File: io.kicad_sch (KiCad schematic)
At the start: 2 parts

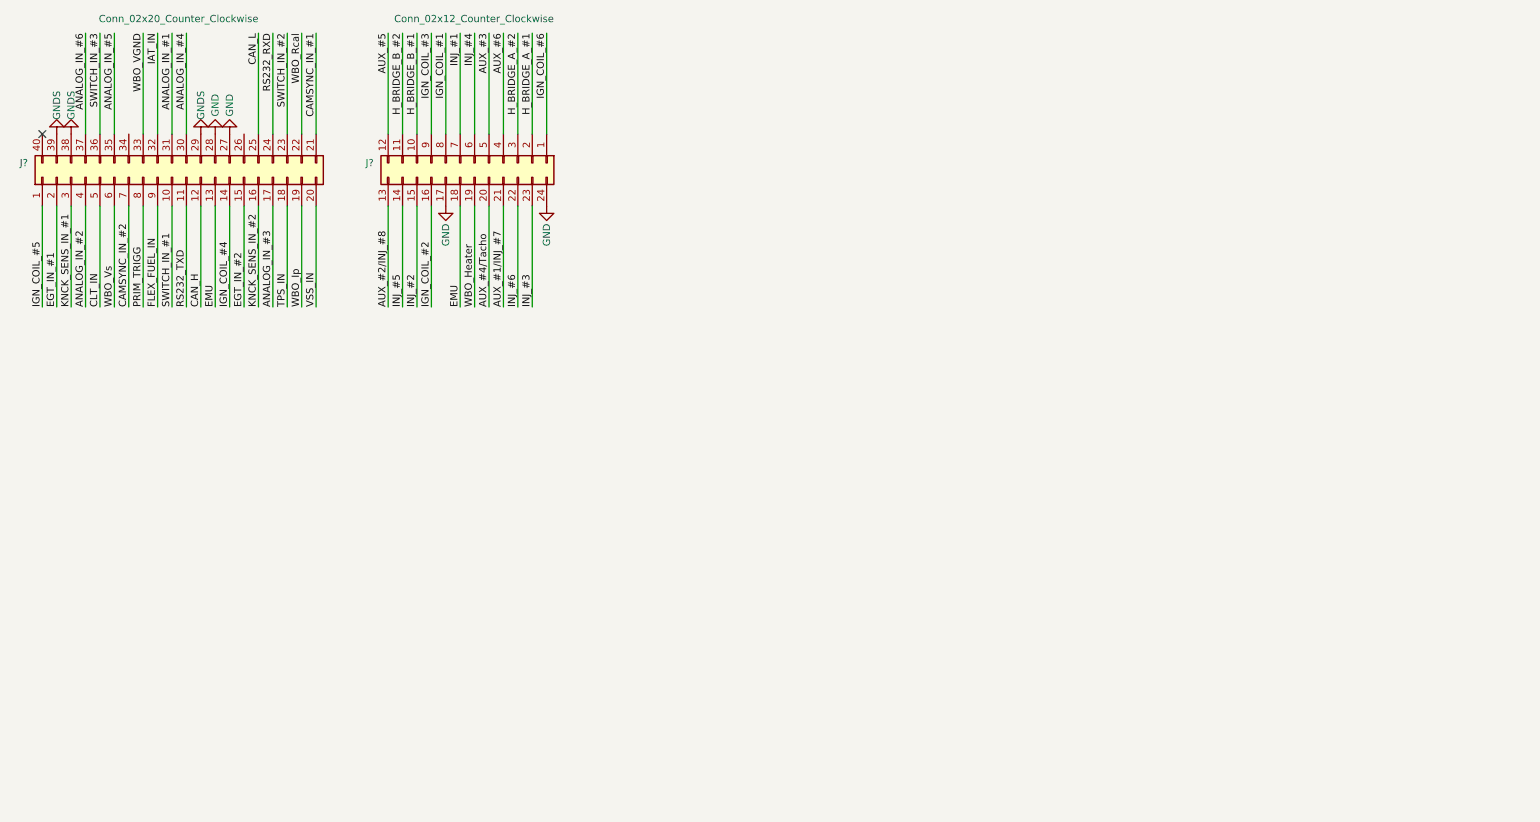
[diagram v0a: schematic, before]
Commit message: Expanded IO
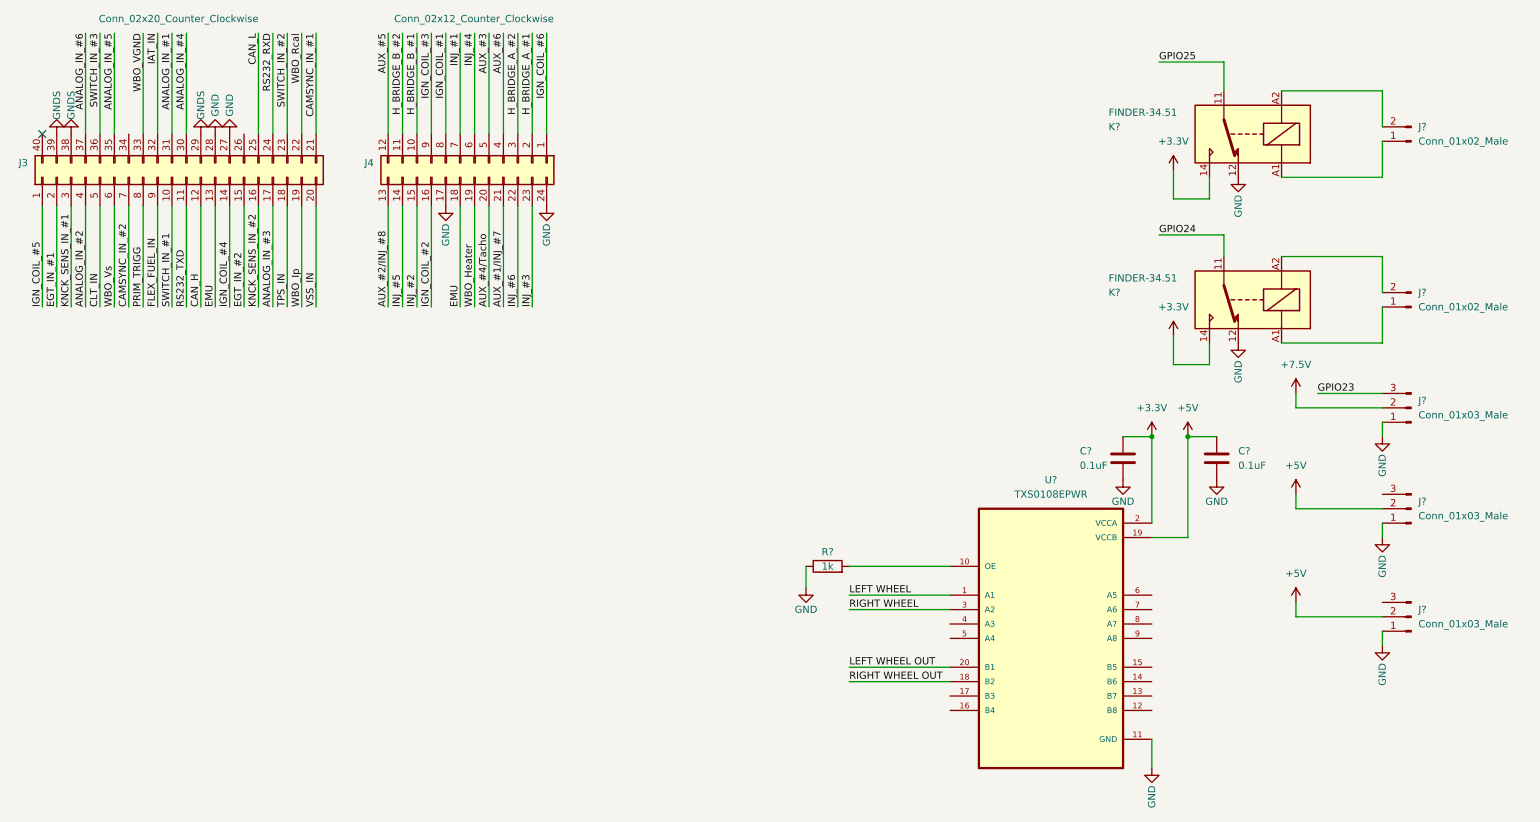
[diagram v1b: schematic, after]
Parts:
- added C? (x2): 0.1uF, symbol Device:C
- added J? (x2): Conn_01x02_Male, symbol Connector:Conn_01x02_Male
- added J? (x3): Conn_01x03_Male, symbol Connector:Conn_01x03_Male
- added K? (x2): FINDER-34.51, Relay_THT:Relay_SPDT_Finder_34.51_Vertical, symbol Relay:FINDER-34.51
- added R?: 1k, symbol Device:R
- added U?: TXS0108EPWR, SOP65P640X120-20N, symbol TXS0108EPWR:TXS0108EPWR
- gave numbers to parts that had none: 2
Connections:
- net GND: now also C?.1, C?.1, J?.1 (Pin_1), J?.1 (Pin_1), J?.1 (Pin_1), K?.12, K?.12, R?.1, U?.11 (GND)
- new net: J?.1 (Pin_1), K?.A1 (x2)
- new net: J?.2 (Pin_2), K?.A2 (x2)
- new net: R?.2, U?.10 (OE)
- new net +3.3V: C?.2, K?.14, K?.14, U?.2 (VCCA)
- new net +5V: C?.2, J?.2 (Pin_2), J?.2 (Pin_2), U?.19 (VCCB)
- new net +7.5V: J?.2 (Pin_2)
- new net GPIO23: J?.3 (Pin_3)
- new net GPIO24: K?.11
- new net GPIO25: K?.11
- new net LEFT WHEEL: U?.1 (A1)
- new net LEFT WHEEL OUT: U?.20 (B1)
- new net RIGHT WHEEL: U?.3 (A2)
- new net RIGHT WHEEL OUT: U?.18 (B2)

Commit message: Rev 1.0
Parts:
- added D10, D9: ES1J, ES1J:DIO_ES1J, symbol ES1J:ES1J
- added J11: STARTER CON, AMASS_XT60PW-F:AMASS_XT60PW-F, symbol XT60PW-F:XT60PW-F
- added J12, J13: USB_C_Receptacle, Connector_USB:USB_C_Receptacle_HRO_TYPE-C-31-M-12, symbol Connector:USB_C_Receptacle
- added J14: CAN, Connector_Molex:Molex_PicoBlade_53047-0210_1x02_P1.25mm_Vertical, symbol Connector:Conn_01x02_Male
- added J15: 3.3V OUT, Connector_Molex:Molex_PicoBlade_53047-0210_1x02_P1.25mm_Vertical, symbol Connector:Conn_01x02_Male
- added J16: 5V OUT, Connector_Molex:Molex_PicoBlade_53047-0210_1x02_P1.25mm_Vertical, symbol Connector:Conn_01x02_Male
- added J17: 7.5V OUT, Connector_Molex:Molex_PicoBlade_53047-0210_1x02_P1.25mm_Vertical, symbol Connector:Conn_01x02_Male
- added J18: OIL CON, Connector_Molex:Molex_PicoBlade_53047-0210_1x02_P1.25mm_Vertical, symbol Connector:Conn_01x02_Male
- added J19: IAT CON, Connector_Molex:Molex_PicoBlade_53047-0210_1x02_P1.25mm_Vertical, symbol Connector:Conn_01x02_Male
- added J20: PRIM TRIGG CON, Connector_Molex:Molex_PicoBlade_53047-0210_1x02_P1.25mm_Vertical, symbol Connector:Conn_01x02_Male
- added J21: SEC TRIGG CON, Connector_Molex:Molex_PicoBlade_53047-0210_1x02_P1.25mm_Vertical, symbol Connector:Conn_01x02_Male
- added J22: EGT CON, Connector_Molex:Molex_PicoBlade_53047-0210_1x02_P1.25mm_Vertical, symbol Connector:Conn_01x02_Male
- added J23: DATA LOGGER CON, Connector_Molex:Molex_PicoBlade_53047-0310_1x03_P1.25mm_Vertical, symbol Connector:Conn_01x03_Male
- added J24: IGN CON, Connector_Molex:Molex_PicoBlade_53047-0310_1x03_P1.25mm_Vertical, symbol Connector:Conn_01x03_Male
- added J25: INJ CON, Connector_Molex:Molex_PicoBlade_53047-0210_1x02_P1.25mm_Vertical, symbol Connector:Conn_01x02_Male
- added K3: FINDER-34.51 INJ, Relay_THT:Relay_SPDT_Finder_34.51_Vertical, symbol Relay:FINDER-34.51
- added Q2, Q3, Q4: IRFP1405PBF, IRFP1405:TO247AC, symbol IRFP1405:IRFP1405PBF
- added R16: 330, Resistor_SMD:R_0603_1608Metric, symbol Device:R
- added U8: 2EDN7524F, 2EDN7524F:SOIC127P600X175-8N-22-V, symbol 2EDN7524F:2EDN7524F
- C15, C16: renamed from C?; footprint (none) -> Capacitor_SMD:C_0201_0603Metric
- J10: renamed from J?; value Conn_01x03_Male -> RIGHT WHEEL SENS; footprint (none) -> Connector_Molex:Molex_PicoBlade_53047-0310_1x03_P1.25mm_Vertical
- J3: value Conn_02x20_Counter_Clockwise -> EMU_BLACK_A; footprint (none) -> Connector_PinHeader_2.54mm:PinHeader_2x20_P2.54mm_Vertical
- J4: value Conn_02x12_Counter_Clockwise -> EMU_BLACK_B; footprint (none) -> Connector_PinHeader_2.54mm:PinHeader_2x12_P2.54mm_Vertical
- J6: renamed from J?; value Conn_01x02_Male -> INJ CON; footprint (none) -> Connector_Molex:Molex_PicoBlade_53047-0210_1x02_P1.25mm_Vertical
- J7: renamed from J?; value Conn_01x02_Male -> STARTER INF; footprint (none) -> Connector_Molex:Molex_PicoBlade_53047-0210_1x02_P1.25mm_Vertical
- J8: renamed from J?; value Conn_01x03_Male -> SERVO; footprint (none) -> Connector_Molex:Molex_PicoBlade_53047-0310_1x03_P1.25mm_Vertical
- J9: renamed from J?; value Conn_01x03_Male -> LEFT WHEEL SENS; footprint (none) -> Connector_Molex:Molex_PicoBlade_53047-0310_1x03_P1.25mm_Vertical
- K1: renamed from K?; value FINDER-34.51 -> FINDER-34.51 INJ
- K2: renamed from K?; value FINDER-34.51 -> FINDER-34.51 STARTER
- R14: renamed from R?; footprint (none) -> Resistor_SMD:R_0603_1608Metric
- U7: renamed from U?; footprint SOP65P640X120-20N -> TXS0108EPWR:SOP65P640X120-20N
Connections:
- net +3.3V: now also J15.2 (Pin_2)
- net +5V: now also J16.2 (Pin_2), U8.6 (VDD)
- net +7.5V: now also J17.2 (Pin_2)
- net ANALOG_IN_#1: now also J18.2 (Pin_2), R16.1
- net CAMSYNC_IN_#1: now also J21.2 (Pin_2)
- net CAN_H: now also J14.1 (Pin_1)
- net CAN_L: now also J14.2 (Pin_2)
- net EGT_IN_#1: now also J22.2 (Pin_2)
- net GND: now also J15.1 (Pin_1), J16.1 (Pin_1), J17.1 (Pin_1), J24.1 (Pin_1), Q2.3 (S), Q3.3 (S), Q4.3 (S)
- net GNDS: now also J18.1 (Pin_1), J19.1 (Pin_1), J20.1 (Pin_1), J21.1 (Pin_1), J22.1 (Pin_1), J23.3 (Pin_3)
- net IAT_IN: now also J19.2 (Pin_2)
- net IGN_COIL_#1: now also J24.2 (Pin_2)
- net INJ_#1: now also K3.14
- net LEFT WHEEL OUT: now also J9.3 (Pin_3)
- net PRIM_TRIGG: now also J20.2 (Pin_2)
- net RIGHT WHEEL OUT: now also J10.3 (Pin_3)
- net RS232_TXD: now also J23.2 (Pin_2)
- net INJ IN: now reaches J6.1 (Pin_1), K1.A1
- net INJ IN: now also D9.K, K3.A1
- net INJ OUT: now reaches J6.2 (Pin_2), K1.A2
- net INJ OUT: now also D9.A, K3.A2
- net at J7.1 (Pin_1), K2.A1: now also D10.K
- net at J7.2 (Pin_2), K2.A2: now also D10.A
- net 5V EMU: now reaches J3.26 (Pin_26)
- net 5V EMU: now also J3.34 (Pin_34), J23.1 (Pin_1), R16.2
- new net: Q2.1 (G), Q3.1 (G), Q4.1 (G), U8.7 (OUTA)
- new net: J11.2, Q2.2 (D), Q3.2 (D), Q4.2 (D)
- new net: J11.S1 (SHIELD), J11.S2 (SHIELD)
- new net: J25.1 (Pin_1), K3.11
- new net: J12.A1 (GND), J12.A12 (GND), J12.B1 (GND), J12.B12 (GND), J12.S1 (SHIELD)
- new net GPIO22: U8.2 (INA)
- new net IGN: J24.3 (Pin_3)
- new net INJ: J25.2 (Pin_2)
- new net STARTER: J11.1
- new net USB_PASSTHROUH_DN: J12.A7 (D-), J12.B7 (D-), J13.A7 (D-), J13.B7 (D-)
- new net USB_PASSTHROUH_DP: J12.A6 (D+), J12.B6 (D+), J13.A6 (D+), J13.B6 (D+)
- new net USB_PASSTHROUH_GND: J13.A1 (GND), J13.A12 (GND), J13.B1 (GND), J13.B12 (GND), J13.S1 (SHIELD)
- new net USB_PASSTHROUH_VSYS: J12.A4 (VBUS), J12.A9 (VBUS), J12.B4 (VBUS), J12.B9 (VBUS), J13.A4 (VBUS), J13.A9 (VBUS), J13.B4 (VBUS), J13.B9 (VBUS)
- no-connect marks 1 -> 19
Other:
- title: (none) -> Iron Warriors v2.0 
- moved on the sheet: C15, C16, J10, J6, J7, J8, J9, K1, K2, R14, U7

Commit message: Initial PCB view
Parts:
- C15, C16: footprint Capacitor_SMD:C_0201_0603Metric -> Capacitor_SMD:C_0603_1608Metric
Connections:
- net RIGHT WHEEL is gone; now on net GPIO22: U7.3 (A2)
- net GPIO22: no longer U8.2 (INA)
- net GPIO23: now also U8.2 (INA); no longer J8.3 (Pin_3)
- net LEFT WHEEL renamed GPIO21
- new net GPIO20: J8.3 (Pin_3)
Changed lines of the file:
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@@
   (title_block
     (title "Iron Warriors v2.0 ")
-    (date "2022-12-08")
+    (date "2022-12-13")
     (rev "1.0")
   )
@@
     (stroke (width 0) (type default) (color 0 0 0 0))
   )
-  (wire (pts (xy 365.76 113.03) (xy 365.76 115.57))
-    (stroke (width 0) (type default) (color 0 0 0 0))
-  )
   (wire (pts (xy 344.17 78.74) (xy 350.52 78.74))
     (stroke (width 0) (type default) (color 0 0 0 0))
@@
     (stroke (width 0) (type default) (color 0 0 0 0))
   )
+  (wire (pts (xy 359.41 113.665) (xy 359.41 115.57))
+    (stroke (width 0) (type default) (color 0 0 0 0))
+  )
   (wire (pts (xy 326.39 179.07) (xy 326.39 173.99))
     (stroke (width 0) (type default) (color 0 0 0 0))
@@
     (stroke (width 0) (type default) (color 0 0 0 0))
   )
+  (wire (pts (xy 273.05 148.59) (xy 290.83 148.59))
+    (stroke (width 0) (type default) (color 0 0 0 0))
+  )
   (wire (pts (xy 381 157.48) (xy 381 154.94))
     (stroke (width 0) (type default) (color 0 0 0 0))
@@
     (stroke (width 0) (type default) (color 0 0 0 0))
   )
+  (wire (pts (xy 273.05 151.13) (xy 290.83 151.13))
+    (stroke (width 0) (type default) (color 0 0 0 0))
+  )
   (wire (pts (xy 323.85 209.55) (xy 340.36 209.55))
     (stroke (width 0) (type default) (color 0 0 0 0))
@@
     (stroke (width 0) (type default) (color 0 0 0 0))
   )
-  (wire (pts (xy 273.05 148.59) (xy 290.83 148.59))
-    (stroke (width 0) (type default) (color 0 0 0 0))
-  )
   (wire (pts (xy 195.58 43.18) (xy 195.58 25.4))
     (stroke (width 0) (type default) (color 0 0 0 0))
@@
     (stroke (width 0) (type default) (color 0 0 0 0))
   )
-  (wire (pts (xy 365.76 115.57) (xy 381 115.57))
-    (stroke (width 0) (type default) (color 0 0 0 0))
-  )
   (wire (pts (xy 107.95 68.58) (xy 107.95 50.8))
     (stroke (width 0) (type default) (color 0 0 0 0))
@@
     (stroke (width 0) (type default) (color 0 0 0 0))
   )
-  (wire (pts (xy 265.43 147.32) (xy 265.43 143.51))
+  (wire (pts (xy 257.81 147.32) (xy 257.81 143.51))
     (stroke (width 0) (type default) (color 0 0 0 0))
   )
@@
     (stroke (width 0) (type default) (color 0 0 0 0))
   )
-  (wire (pts (xy 265.43 143.51) (xy 270.51 143.51))
+  (wire (pts (xy 257.81 143.51) (xy 270.51 143.51))
     (stroke (width 0) (type default) (color 0 0 0 0))
   )
@@
     (stroke (width 0) (type default) (color 0 0 0 0))
   )
-  (wire (pts (xy 273.05 151.13) (xy 290.83 151.13))
-    (stroke (width 0) (type default) (color 0 0 0 0))
-  )
   (wire (pts (xy 208.28 43.18) (xy 208.28 25.4))
     (stroke (width 0) (type default) (color 0 0 0 0))
@@
     (stroke (width 0) (type default) (color 0 0 0 0))
   )
+  (wire (pts (xy 359.41 115.57) (xy 381 115.57))
+    (stroke (width 0) (type default) (color 0 0 0 0))
+  )
   (wire (pts (xy 71.12 96.52) (xy 46.99 96.52))
     (stroke (width 0) (type default) (color 0 0 0 0))
@@
     (effects (font (size 1.27 1.27)) (justify left bottom))
   )
-  (label "RIGHT WHEEL" (at 273.05 151.13 0)
+  (label "GPIO22" (at 273.05 151.13 0)
     (effects (font (size 1.27 1.27)) (justify left bottom))
   )
@@
     (effects (font (size 1.27 1.27)) (justify right bottom))
   )
-  (label "LEFT WHEEL" (at 273.05 148.59 0)
-    (effects (font (size 1.27 1.27)) (justify left bottom))
-  )
   (label "IGN_COIL_#1" (at 92.71 20.32 270)
     (effects (font (size 1.27 1.27)) (justify right bottom))
@@
     (effects (font (size 1.27 1.27)) (justify right bottom))
   )
+  (label "GPIO21" (at 273.05 148.59 0)
+    (effects (font (size 1.27 1.27)) (justify left bottom))
+  )
   (label "INJ_#5" (at 85.09 68.58 90)
     (effects (font (size 1.27 1.27)) (justify left bottom))
@@
     (effects (font (size 1.27 1.27)) (justify left bottom))
   )
-  (label "GPIO22" (at 279.4 209.55 0)
+  (label "GPIO23" (at 279.4 209.55 0)
     (effects (font (size 1.27 1.27)) (justify left bottom))
   )
@@
     (effects (font (size 1.27 1.27)) (justify left bottom))
   )
-  (label "GPIO23" (at 369.57 113.03 0)
+  (label "GPIO20" (at 369.57 113.03 0)
     (effects (font (size 1.27 1.27)) (justify left bottom))
   )
@@
   (label "5V EMU" (at 36.83 20.32 270)
     (effects (font (size 1.27 1.27)) (justify right bottom))
+  )
+  (hierarchical_label "EMU" (shape input) (at 52.07 68.58 270)
+    (effects (font (size 1.27 1.27)) (justify right))
+  )
+  (hierarchical_label "GPIO25" (shape output) (at 341.63 54.61 180)
+    (effects (font (size 1.27 1.27)) (justify right))
+  )
+  (hierarchical_label "GPIO22" (shape output) (at 273.05 151.13 180)
+    (effects (font (size 1.27 1.27)) (justify right))
+  )
+  (hierarchical_label "IGN" (shape input) (at 260.35 43.18 270)
+    (effects (font (size 1.27 1.27)) (justify right))
+  )
+  (hierarchical_label "EMU" (shape input) (at 95.25 68.58 270)
+    (effects (font (size 1.27 1.27)) (justify right))
+  )
+  (hierarchical_label "STARTER" (shape input) (at 367.03 181.61 180)
+    (effects (font (size 1.27 1.27)) (justify right))
+  )
+  (hierarchical_label "GPIO23" (shape input) (at 279.4 209.55 180)
+    (effects (font (size 1.27 1.27)) (justify right))
+  )
+  (hierarchical_label "INJ" (shape input) (at 354.33 16.51 90)
+    (effects (font (size 1.27 1.27)) (justify left))
+  )
+  (hierarchical_label "GPIO20" (shape input) (at 369.57 113.03 180)
+    (effects (font (size 1.27 1.27)) (justify right))
+  )
+  (hierarchical_label "GPIO24" (shape output) (at 341.63 85.09 180)
+    (effects (font (size 1.27 1.27)) (justify right))
+  )
+  (hierarchical_label "GPIO21" (shape output) (at 273.05 148.59 180)
+    (effects (font (size 1.27 1.27)) (justify right))
   )
   (symbol (lib_id "Connector:Conn_01x02_Male") (at 386.08 68.58 180) (unit 1)
@@
       (effects (font (size 1.27 1.27)) (justify right))
     )
-    (property "Footprint" "Capacitor_SMD:C_0201_0603Metric" (id 2) (at 320.3448 120.65 0)
+    (property "Footprint" "Capacitor_SMD:C_0603_1608Metric" (id 2) (at 320.3448 120.65 0)
       (effects (font (size 1.27 1.27)) hide)
     )
@@
       (effects (font (size 1.27 1.27)) (justify right))
     )
-    (property "Footprint" "Capacitor_SMD:C_0201_0603Metric" (id 2) (at 336.8548 120.65 0)
+    (property "Footprint" "Capacitor_SMD:C_0603_1608Metric" (id 2) (at 336.8548 120.65 0)
       (effects (font (size 1.27 1.27)) hide)
     )
@@
     (pin "9")
   )
-  (symbol (lib_id "power:+7.5V") (at 365.76 113.03 0) (unit 1)
+  (symbol (lib_id "power:+7.5V") (at 359.41 113.665 0) (unit 1)
     (in_bom yes) (on_board yes) (fields_autoplaced)
-    (property "Reference" "#PWR031" (id 0) (at 365.76 116.84 0)
-      (effects (font (size 1.27 1.27)) hide)
-    )
-    (property "Value" "+7.5V" (id 1) (at 365.76 107.95 0))
-    (property "Footprint" "" (id 2) (at 365.76 113.03 0)
-      (effects (font (size 1.27 1.27)) hide)
-    )
-    (property "Datasheet" "" (id 3) (at 365.76 113.03 0)
+    (property "Reference" "#PWR031" (id 0) (at 359.41 117.475 0)
+      (effects (font (size 1.27 1.27)) hide)
+    )
+    (property "Value" "+7.5V" (id 1) (at 359.41 108.585 0))
+    (property "Footprint" "" (id 2) (at 359.41 113.665 0)
+      (effects (font (size 1.27 1.27)) hide)
+    )
+    (property "Datasheet" "" (id 3) (at 359.41 113.665 0)
       (effects (font (size 1.27 1.27)) hide)
     )
@@
     (pin "1")
   )
-  (symbol (lib_id "power:GND") (at 265.43 147.32 0) (unit 1)
-    (in_bom yes) (on_board yes)
-    (property "Reference" "#PWR021" (id 0) (at 265.43 153.67 0)
-      (effects (font (size 1.27 1.27)) hide)
-    )
-    (property "Value" "GND" (id 1) (at 265.43 151.13 0))
-    (property "Footprint" "" (id 2) (at 265.43 147.32 0)
-      (effects (font (size 1.27 1.27)) hide)
-    )
-    (property "Datasheet" "" (id 3) (at 265.43 147.32 0)
-      (effects (font (size 1.27 1.27)) hide)
-    )
+  (symbol (lib_id "power:GND") (at 257.81 147.32 0) (unit 1)
+    (in_bom yes) (on_board yes)
+    (property "Reference" "#PWR021" (id 0) (at 257.81 153.67 0)
+      (effects (font (size 1.27 1.27)) hide)
+    )
+    (property "Value" "GND" (id 1) (at 257.81 151.13 0))
+    (property "Footprint" "" (id 2) (at 257.81 147.32 0)
+      (effects (font (size 1.27 1.27)) hide)
+    )
+    (property "Datasheet" "" (id 3) (at 257.81 147.32 0)
+      (effects (font (size 1.27 1.27)) hide)
+    )

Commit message: First full version of the PCB
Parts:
- J10, J23, J24, J8, J9: footprint Connector_Molex:Molex_PicoBlade_53047-0310_1x03_P1.25mm_Vertical -> TerminalBlock_Phoenix:TerminalBlock_Phoenix_MPT-0,5-3-2.54_1x03_P2.54mm_Horizontal
- J14, J15, J16, J17, J18, J19, J20, J21, J22, J25, J6, J7: footprint Connector_Molex:Molex_PicoBlade_53047-0210_1x02_P1.25mm_Vertical -> TerminalBlock_Phoenix:TerminalBlock_Phoenix_MPT-0,5-2-2.54_1x02_P2.54mm_Horizontal
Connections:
- net USB_PASSTHROUH_GND: now also J12.A1 (GND), J12.A12 (GND), J12.B1 (GND), J12.B12 (GND), J12.S1 (SHIELD)
- no-connect marks 19 -> 43

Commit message: Small corrections
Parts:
- removed D10, D9: ES1J, ES1J:DIO_ES1J, symbol ES1J:ES1J
- added D10, D9: SS14, Diode_SMD:D_SMA, symbol Device:D_Schottky
- added J26: MAP, TerminalBlock_Phoenix:TerminalBlock_Phoenix_MPT-0,5-2-2.54_1x02_P2.54mm_Horizontal, symbol Connector:Conn_01x02_Male
- added J27: CLT CON, TerminalBlock_Phoenix:TerminalBlock_Phoenix_MPT-0,5-2-2.54_1x02_P2.54mm_Horizontal, symbol Connector:Conn_01x02_Male
- added R17: 330, Resistor_SMD:R_0603_1608Metric, symbol Device:R
- J3: footprint Connector_PinHeader_2.54mm:PinHeader_2x20_P2.54mm_Vertical -> Connector_IDC:IDC-Header_2x20_P2.54mm_Vertical
- J4: footprint Connector_PinHeader_2.54mm:PinHeader_2x12_P2.54mm_Vertical -> Connector_IDC:IDC-Header_2x12_P2.54mm_Vertical
- J6: value INJ CON -> INJ_&_STARTER
- J7: value STARTER INF -> 16V OUT
- R14: value 1k -> 10k
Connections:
- net INJ OUT is gone; now on net INJ IN: J6.2 (Pin_2), K1.A2, K3.A2
- net VSS_IN is gone; now on net RIGHT WHEEL OUT: J3.20 (Pin_20)
- net +3.3V: now also R14.2, U7.10 (OE)
- net +5V: now also J23.1 (Pin_1)
- net 5V EMU: now also R17.2; no longer J23.1 (Pin_1)
- net ANALOG_IN_#4: now also J26.2 (Pin_2)
- net CLT_IN: now also J27.2 (Pin_2), R17.1
- net GND: now also J23.3 (Pin_3), J7.1 (Pin_1), K1.A1, K2.A1, K3.A1, U8.3 (GND), D10.2 (A), D9.2 (A), J26.1 (Pin_1)
- net GNDS: now also J27.1 (Pin_1); no longer J23.3 (Pin_3)
- net GPIO21: now also K1.11; no longer U7.1 (A1)
- net GPIO22: now also K2.11; no longer U7.3 (A2)
- net GPIO24: now also U7.3 (A2); no longer K2.11
- net GPIO25: now also U7.1 (A1); no longer K1.11
- net INJ IN: now also D9.1 (K); no longer J6.1 (Pin_1), K1.A1, K3.A1
- net at K2.A2: now also J6.1 (Pin_1), D10.1 (K); no longer J7.2 (Pin_2)
- net GPIO23 renamed GPIO10
- new net 16V: J7.2 (Pin_2)
- no-connect marks 43 -> 42
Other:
- moved on the sheet: J14, J15, J16, J17, J18, J19, J20, J21, J22, J23, J24, R16
